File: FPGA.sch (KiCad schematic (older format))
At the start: 39 parts, among them J17 Conn_01x06, SW1601 SW_Push, U1601 ICE40HX1K-4K-TQ144, U1603 ASDMB-xxxMHz, U5 M25PX32-VMW

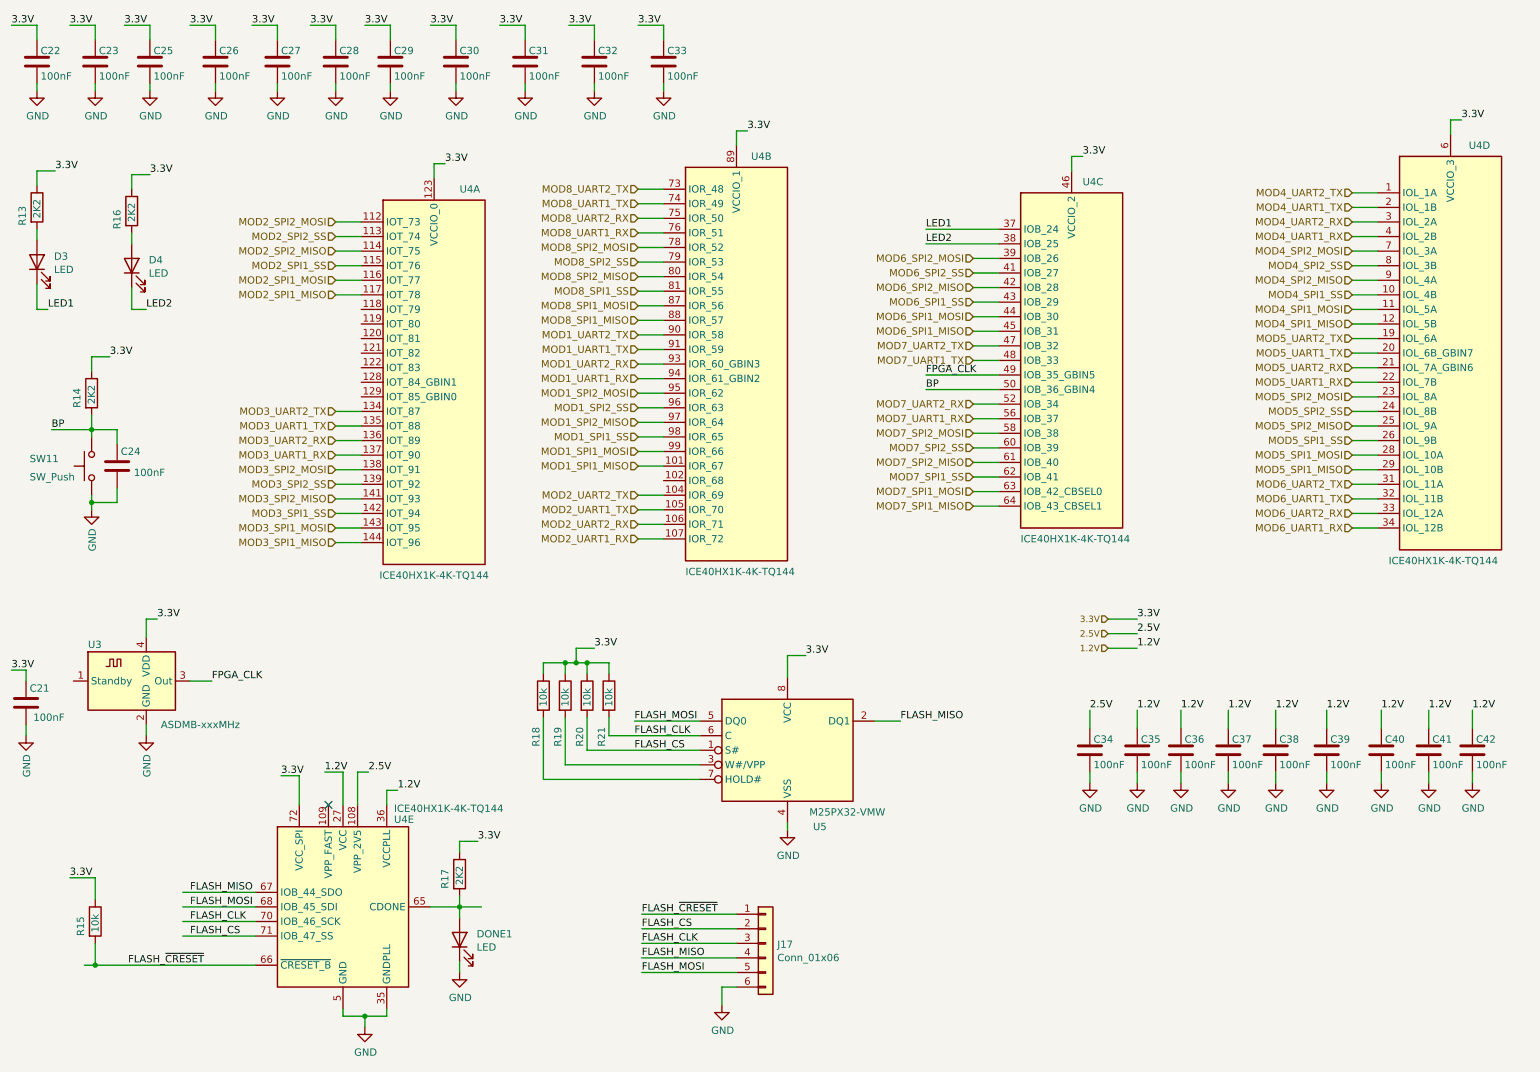
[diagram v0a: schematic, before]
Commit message: Most PSB done, needs more silk screen cosmetic plus review
Signed-off-by: Alexis Jeandet <alexis.jeandet@member.fsf.org>
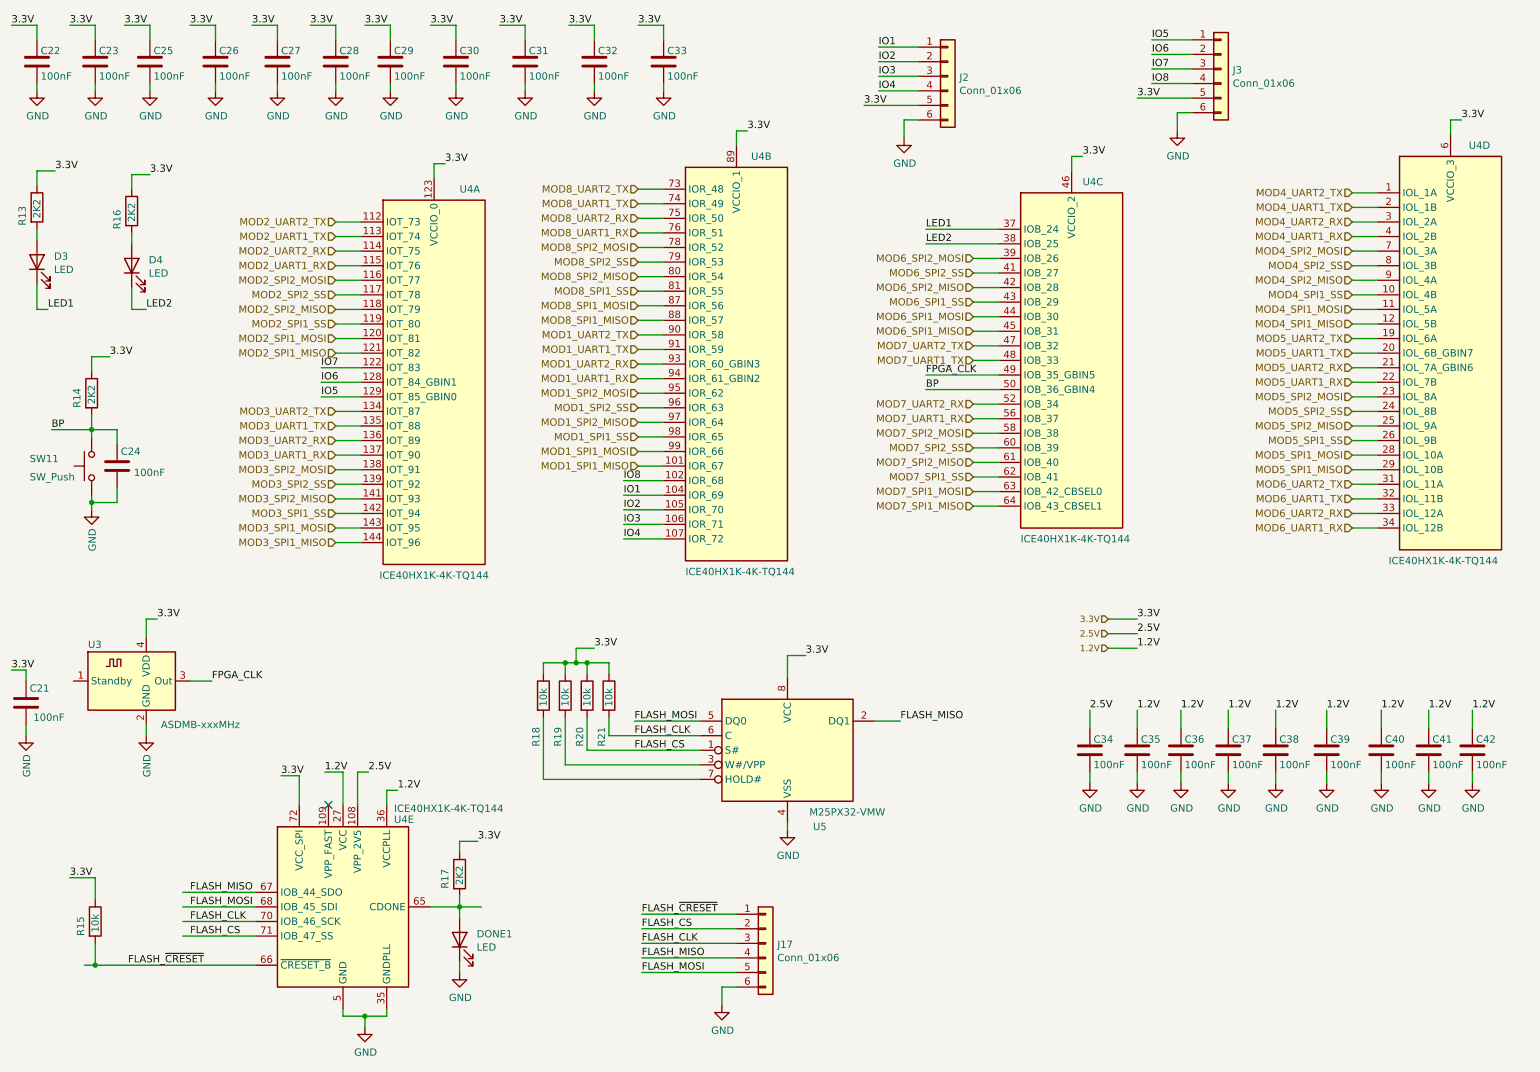
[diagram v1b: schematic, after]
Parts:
- added J2, J3: Conn_01x06, Connector_PinHeader_2.54mm:PinHeader_1x06_P2.54mm_Vertical, symbol Connector_Generic:Conn_01x06
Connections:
- net GND: now also J2.6 (Pin_6), J3.6 (Pin_6)
- net MOD2_SPI1_MISO: now also U1601.121 (IOT_82); no longer U1601.117 (IOT_78)
- net MOD2_SPI1_MOSI: now also U1601.120 (IOT_81); no longer U1601.116 (IOT_77)
- net MOD2_SPI1_SS: now also U1601.119 (IOT_80); no longer U1601.115 (IOT_76)
- net MOD2_SPI2_MISO: now also U1601.118 (IOT_79); no longer U1601.114 (IOT_75)
- net MOD2_SPI2_MOSI: now also U1601.116 (IOT_77); no longer U1601.112 (IOT_73)
- net MOD2_SPI2_SS: now also U1601.117 (IOT_78); no longer U1601.113 (IOT_74)
- net MOD2_UART1_RX: now also U1601.115 (IOT_76); no longer U1601.107 (IOR_72)
- net MOD2_UART1_TX: now also U1601.113 (IOT_74); no longer U1601.105 (IOR_70)
- net MOD2_UART2_RX: now also U1601.114 (IOT_75); no longer U1601.106 (IOR_71)
- net MOD2_UART2_TX: now also U1601.112 (IOT_73); no longer U1601.104 (IOR_69)
- net VCCIO_0: now also J2.5 (Pin_5), J3.5 (Pin_5)
- net IO7: now reaches U1601.122 (IOT_83)
- net IO7: now also J3.3 (Pin_3)
- net IO6: now reaches U1601.128 (IOT_84_GBIN1)
- net IO6: now also J3.2 (Pin_2)
- net IO5: now reaches U1601.129 (IOT_85_GBIN0)
- net IO5: now also J3.1 (Pin_1)
- net IO8: now reaches U1601.102 (IOR_68)
- net IO8: now also J3.4 (Pin_4)
- new net IO1: J2.1 (Pin_1), U1601.104 (IOR_69)
- new net IO2: J2.2 (Pin_2), U1601.105 (IOR_70)
- new net IO3: J2.3 (Pin_3), U1601.106 (IOR_71)
- new net IO4: J2.4 (Pin_4), U1601.107 (IOR_72)
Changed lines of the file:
@@
 Wire Wire Line
 	5250 2800 5075 2800
+Text HLabel 3000 2825 0    50   Input ~ 0
+MOD2_SPI1_MOSI
+Text HLabel 3000 2925 0    50   Input ~ 0
+MOD2_SPI1_MISO
+Text HLabel 3000 2725 0    50   Input ~ 0
+MOD2_SPI1_SS
 Text HLabel 3000 2425 0    50   Input ~ 0
-MOD2_SPI1_MOSI
+MOD2_SPI2_MOSI
+Text HLabel 3000 2625 0    50   Input ~ 0
+MOD2_SPI2_MISO
 Text HLabel 3000 2525 0    50   Input ~ 0
-MOD2_SPI1_MISO
+MOD2_SPI2_SS
+Text HLabel 3000 2125 0    50   Input ~ 0
+MOD2_UART1_TX
 Text HLabel 3000 2325 0    50   Input ~ 0
-MOD2_SPI1_SS
+MOD2_UART1_RX
 Text HLabel 3000 2025 0    50   Input ~ 0
-MOD2_SPI2_MOSI
+MOD2_UART2_TX
 Text HLabel 3000 2225 0    50   Input ~ 0
-MOD2_SPI2_MISO
-Text HLabel 3000 2125 0    50   Input ~ 0
-MOD2_SPI2_SS
-Text HLabel 5075 4000 0    50   Input ~ 0
-MOD2_UART1_TX
-Text HLabel 5075 4200 0    50   Input ~ 0
-MOD2_UART1_RX
-Text HLabel 5075 3900 0    50   Input ~ 0
-MOD2_UART2_TX
-Text HLabel 5075 4100 0    50   Input ~ 0
 MOD2_UART2_RX
 Text HLabel 3000 4125 0    50   Input ~ 0
@@
 MOD3_UART2_RX
 Wire Wire Line
-	5250 4200 5075 4200
-Wire Wire Line
-	5250 4100 5075 4100
-Wire Wire Line
-	5250 4000 5075 4000
-Wire Wire Line
-	5250 3900 5075 3900
+	3175 2325 3000 2325
+Wire Wire Line
+	3175 2225 3000 2225
+Wire Wire Line
+	3175 2125 3000 2125
+Wire Wire Line
+	3175 2025 3000 2025
+Wire Wire Line
+	3175 2925 3000 2925
+Wire Wire Line
+	3175 2825 3000 2825
+Wire Wire Line
+	3175 2725 3000 2725
+Wire Wire Line
+	3175 2625 3000 2625
 Wire Wire Line
 	3175 2525 3000 2525
 Wire Wire Line
 	3175 2425 3000 2425
-Wire Wire Line
-	3175 2325 3000 2325
-Wire Wire Line
-	3175 2225 3000 2225
-Wire Wire Line
-	3175 2125 3000 2125
-Wire Wire Line
-	3175 2025 3000 2025
 Wire Wire Line
 	3175 4225 3000 4225
@@
 Wire Wire Line
 	5250 1800 5075 1800
+$Comp
+L Connector_Generic:Conn_01x06 J2
+U 1 1 5F984670
+P 7200 1025
+F 0 "J2" H 7280 1017 50  0000 L CNN
+F 1 "Conn_01x06" H 7280 926 50  0000 L CNN
+F 2 "Connector_PinHeader_2.54mm:PinHeader_1x06_P2.54mm_Vertical" H 7200 1025 50  0001 C CNN
+F 3 "~" H 7200 1025 50  0001 C CNN
+	1    7200 1025
+	1    0    0    -1
+$EndComp
+$Comp
+L power:GND #PWR?
+U 1 1 5F9A2119
+P 6900 1450
+AR Path="/5E4285EC/5F9A2119" Ref="#PWR?"  Part="1"
+AR Path="/5FC0CE7F/5F9A2119" Ref="#PWR?"  Part="1"
+AR Path="/5F61B694/5F9A2119" Ref="#PWR?"  Part="1"
+AR Path="/5F420A26/5F62EEDC/5F9A2119" Ref="#PWR?"  Part="1"
+AR Path="/5F604EE6/5F9A2119" Ref="#PWR0152"  Part="1"
+F 0 "#PWR0152" H 6900 1200 50  0001 C CNN
+F 1 "GND" H 6905 1277 50  0000 C CNN
+F 2 "" H 6900 1450 50  0001 C CNN
+F 3 "" H 6900 1450 50  0001 C CNN
+	1    6900 1450
+	1    0    0    -1
+$EndComp
+Wire Wire Line
+	6900 1450 6900 1325
+Wire Wire Line
+	6900 1325 7000 1325
+Text Label 6625 1225 0    50   ~ 0
+3.3V
+Wire Wire Line
+	7000 1225 6625 1225
+Wire Wire Line
+	7000 825  6725 825
+Wire Wire Line
+	7000 925  6725 925
+Wire Wire Line
+	7000 1025 6725 1025
+Wire Wire Line
+	7000 1125 6725 1125
+Text Label 6725 825  0    50   ~ 0
+IO1
+Text Label 6725 925  0    50   ~ 0
+IO2
+Text Label 6725 1025 0    50   ~ 0
+IO3
+Text Label 6725 1125 0    50   ~ 0
+IO4
+Wire Wire Line
+	5250 3900 4975 3900
+Wire Wire Line
+	5250 4000 4975 4000
+Wire Wire Line
+	5250 4100 4975 4100
+Wire Wire Line
+	5250 4200 4975 4200
+Text Label 4975 3900 0    50   ~ 0
+IO1
+Text Label 4975 4000 0    50   ~ 0
+IO2
+Text Label 4975 4100 0    50   ~ 0
+IO3
+Text Label 4975 4200 0    50   ~ 0
+IO4
+$Comp
+L Connector_Generic:Conn_01x06 J3
+U 1 1 5FA793BF
+P 9075 975
+F 0 "J3" H 9155 967 50  0000 L CNN
+F 1 "Conn_01x06" H 9155 876 50  0000 L CNN
+F 2 "Connector_PinHeader_2.54mm:PinHeader_1x06_P2.54mm_Vertical" H 9075 975 50  0001 C CNN
+F 3 "~" H 9075 975 50  0001 C CNN
+	1    9075 975
+	1    0    0    -1
+$EndComp
+$Comp
+L power:GND #PWR?
+U 1 1 5FA793C9
+P 8775 1400
+AR Path="/5E4285EC/5FA793C9" Ref="#PWR?"  Part="1"
+AR Path="/5FC0CE7F/5FA793C9" Ref="#PWR?"  Part="1"
+AR Path="/5F61B694/5FA793C9" Ref="#PWR?"  Part="1"
+AR Path="/5F420A26/5F62EEDC/5FA793C9" Ref="#PWR?"  Part="1"
+AR Path="/5F604EE6/5FA793C9" Ref="#PWR0153"  Part="1"
+F 0 "#PWR0153" H 8775 1150 50  0001 C CNN
+F 1 "GND" H 8780 1227 50  0000 C CNN
+F 2 "" H 8775 1400 50  0001 C CNN
+F 3 "" H 8775 1400 50  0001 C CNN
+	1    8775 1400
+	1    0    0    -1
+$EndComp
+Wire Wire Line
+	8775 1400 8775 1275
+Wire Wire Line
+	8775 1275 8875 1275
+Wire Wire Line
+	8875 1175 8500 1175
+Wire Wire Line
+	8875 775  8600 775
+Wire Wire Line
+	8875 875  8600 875
+Wire Wire Line
+	8875 975  8600 975
+Wire Wire Line
+	8875 1075 8600 1075
+Text Label 8500 1175 0    50   ~ 0
+3.3V
+Text Label 8600 775  0    50   ~ 0
+IO5
+Text Label 8600 875  0    50   ~ 0
+IO6
+Text Label 8600 975  0    50   ~ 0
+IO7
+Text Label 8600 1075 0    50   ~ 0
+IO8
+Wire Wire Line
+	3175 3025 2900 3025
+Wire Wire Line
+	3175 3125 2900 3125
+Wire Wire Line
+	3175 3225 2900 3225
+Wire Wire Line
+	5250 3800 4975 3800
+Text Label 2900 3225 0    50   ~ 0
+IO5
+Text Label 2900 3125 0    50   ~ 0
+IO6
+Text Label 2900 3025 0    50   ~ 0
+IO7
+Text Label 4975 3800 0    50   ~ 0
+IO8
 $EndSCHEMATC
